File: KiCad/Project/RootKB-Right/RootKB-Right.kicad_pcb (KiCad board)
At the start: 2 copper layers, 137.4 x 107.4 mm, 70 parts, among them J1 OLED-128x32, SW1 Switch, U1 Arduino_Pro_Micro, U2 TRRS

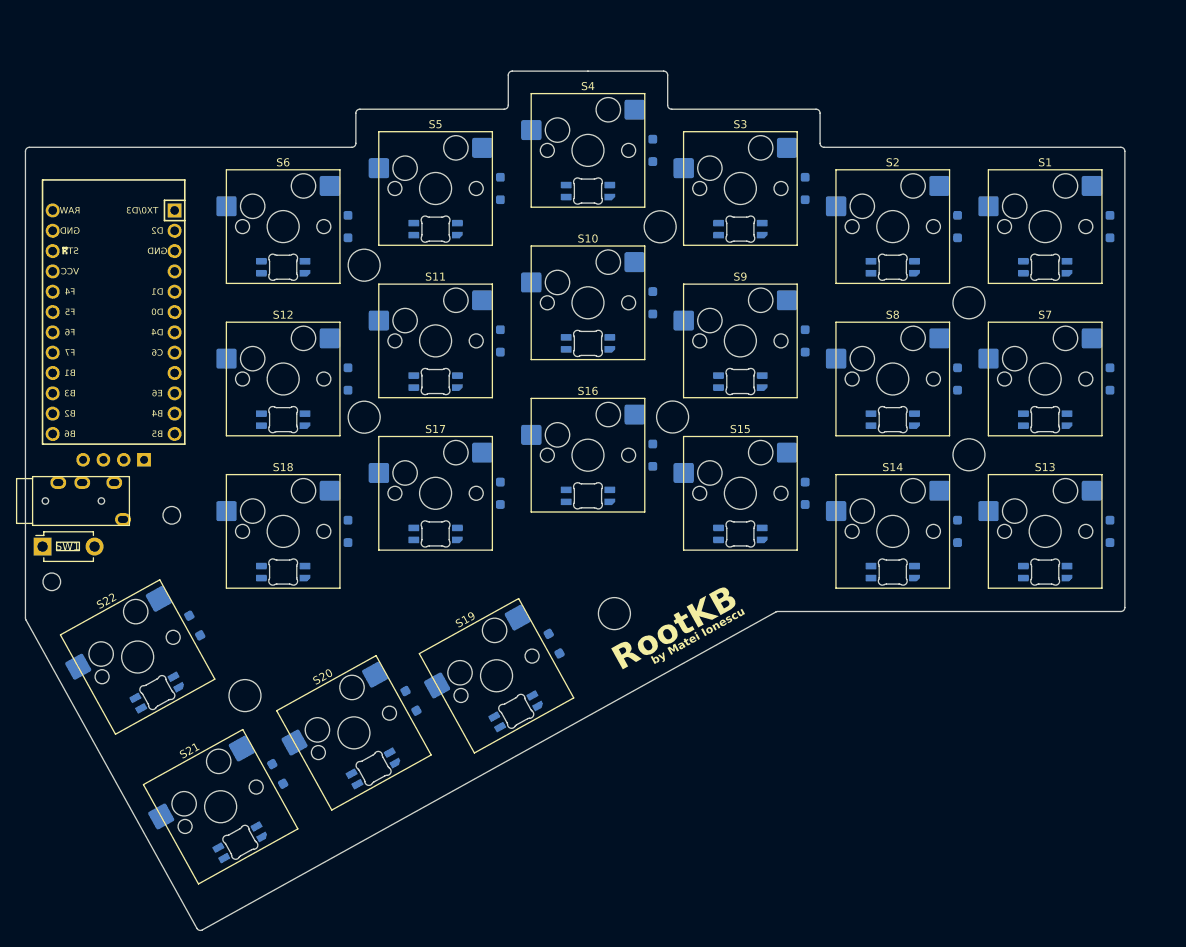
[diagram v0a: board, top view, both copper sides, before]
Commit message: Make symmetrical right PCB
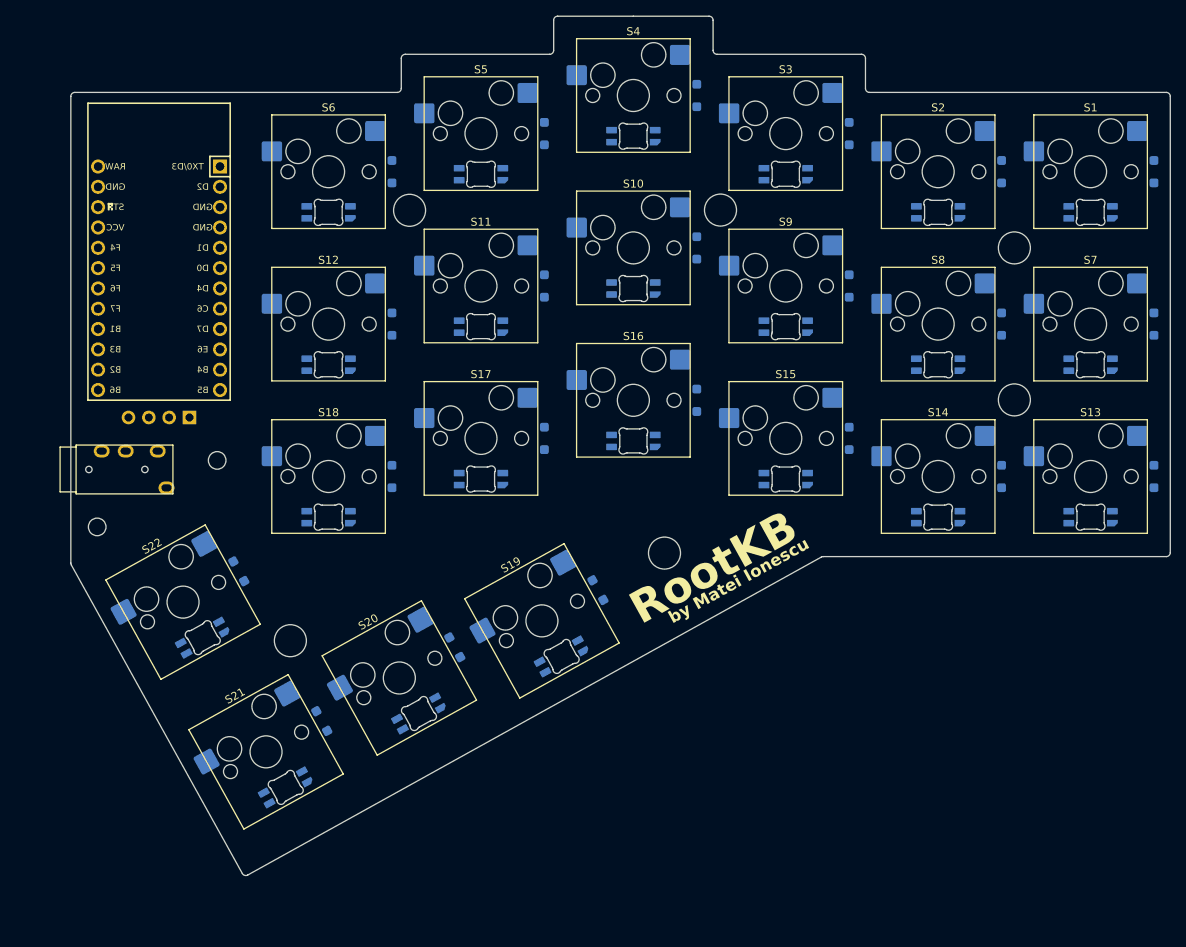
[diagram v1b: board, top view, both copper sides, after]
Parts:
- removed SW1: Switch, ScottoKeebs_Components:Button_MJTP1250
- moved LED21 8.90 mm to (108.8, 136.0)
- moved LED15 8.90 mm to (171.3, 97.4)
- moved LED19 8.90 mm to (143.3, 119.6)
- moved LED3 8.90 mm to (171.3, 59.3)
- moved LED9 8.90 mm to (171.3, 78.4)
- moved S15 8.90 mm to (171.3, 92.3)
- moved S3 8.90 mm to (171.3, 54.2)
- moved S9 8.90 mm to (171.3, 73.3)
- moved S6 8.90 mm to (114.2, 59.0)
- moved LED12 8.90 mm to (114.2, 83.1)
- moved LED18 8.90 mm to (114.2, 102.2)
- moved LED20 8.90 mm to (125.5, 126.7)
- moved LED6 8.90 mm to (114.2, 64.1)
- moved S12 8.90 mm to (114.2, 78.0)
- moved S18 8.90 mm to (114.2, 97.1)
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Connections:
- D10 pad 1: Row 3 -> Row 1
- D11 pad 1: Row 0 -> Row 1
- D14 pad 1: Row 3 -> Row 2
- D15 pad 1: Row 0 -> Row 2
- D16 pad 1: Row 1 -> Row 2
- D18 pad 1: Row 3 -> Row 2
- D19 pad 1: Row 0 -> Row 3
- D2 pad 1: Row 1 -> Row 0
- D20 pad 1: Row 1 -> Row 3
- D21 pad 1: Row 2 -> Row 3
- D3 pad 1: Row 2 -> Row 0
- D5 pad 1: Row 1 -> Row 0
- D6 pad 1: Row 2 -> Row 0
- D7 pad 1: Row 0 -> Row 1
- D9 pad 1: Row 2 -> Row 1
- LED1 pad 3: LED -> Net-(LED1-DIN)
- LED10 pad 2: unconnected-(LED10-DOUT-Pad2) -> Net-(LED10-DOUT)
- LED11 pad 3: Net-(LED11-DIN) -> Net-(LED10-DOUT)
- LED12 pad 3: Net-(LED12-DIN) -> Net-(LED11-DOUT)
- LED14 pad 2: Net-(LED10-DIN) -> Net-(LED13-DIN)
- LED15 pad 2: Net-(LED15-DOUT) -> Net-(LED14-DIN)
- LED15 pad 3: Net-(LED11-DOUT) -> Net-(LED15-DIN)
- LED16 pad 2: Net-(LED12-DIN) -> Net-(LED15-DIN)
- LED17 pad 2: Net-(LED17-DOUT) -> Net-(LED16-DIN)
- LED17 pad 3: Net-(LED13-DOUT) -> Net-(LED17-DIN)
- LED18 pad 2: Net-(LED14-DIN) -> Net-(LED17-DIN)
- LED18 pad 3: Net-(LED18-DIN) -> Net-(LED12-DOUT)
- LED19 pad 3: Net-(LED15-DOUT) -> Net-(LED13-DOUT)
- LED2 pad 2: Net-(LED2-DOUT) -> Net-(LED1-DIN)
- LED20 pad 2: Net-(LED16-DIN) -> Net-(LED20-DOUT)
- LED21 pad 3: Net-(LED17-DOUT) -> Net-(LED20-DOUT)
- LED22 pad 2: Net-(LED18-DIN) -> unconnected-(LED22-DOUT-Pad2)
- LED3 pad 2: Net-(LED3-DOUT) -> Net-(LED2-DIN)
- LED3 pad 3: Net-(LED2-DOUT) -> Net-(LED3-DIN)
- LED3 pad 4: unconnected-(LED3-VSS-Pad4) -> GND
- LED4 pad 2: Net-(LED4-DOUT) -> Net-(LED3-DIN)
- LED4 pad 3: Net-(LED1-DOUT) -> Net-(LED4-DIN)
- LED5 pad 2: Net-(LED2-DIN) -> Net-(LED4-DIN)
- LED6 pad 2: Net-(LED6-DOUT) -> Net-(LED5-DIN)
- LED6 pad 3: Net-(LED3-DOUT) -> LED
- LED6 pad 4: unconnected-(LED6-VSS-Pad4) -> GND
- LED7 pad 2: Net-(LED11-DIN) -> Net-(LED7-DOUT)
- LED7 pad 3: Net-(LED4-DOUT) -> Net-(LED1-DOUT)
- LED8 pad 2: Net-(LED5-DIN) -> Net-(LED8-DOUT)
- LED8 pad 3: Net-(LED12-DOUT) -> Net-(LED7-DOUT)
- LED9 pad 2: Net-(LED13-DIN) -> Net-(LED10-DIN)
- LED9 pad 3: Net-(LED6-DOUT) -> Net-(LED8-DOUT)
- S10 pad 1: Column 2 -> Column 3
- S11 pad 1: Column 3 -> Column 4
- S12 pad 1: Column 3 -> Column 5
- S13 pad 1: Column 3 -> Column 0
- S14 pad 1: Column 3 -> Column 1
- S15 pad 1: Column 4 -> Column 2
- S16 pad 1: Column 4 -> Column 3
- S18 pad 1: Column 4 -> Column 5
- S19 pad 1: Column 5 -> Column 2
- S2 pad 1: Column 0 -> Column 1
- S20 pad 1: Column 5 -> Column 3
- S21 pad 1: Column 5 -> Column 4
- S3 pad 1: Column 0 -> Column 2
- S4 pad 1: Column 1 -> Column 3
- S5 pad 1: Column 1 -> Column 4
- S6 pad 1: Column 1 -> Column 5
- S7 pad 1: Column 2 -> Column 0
- S8 pad 1: Column 2 -> Column 1
- U1 pad 1: unconnected-(U1-TX0/PD3-Pad1) -> TRRS_TX
- U1 pad 13: Column 4 -> Column 1
- U1 pad 14: Column 3 -> Column 2
- U1 pad 15: Column 2 -> Column 3
- U1 pad 16: Column 1 -> Column 4
- U1 pad 2: TRRS_SERIAL -> TRRS_RX
- U1 pad 22: RST -> unconnected-(U1-RST-Pad22)
- U2 pad 1: unconnected-(U2-SLEEVE-Pad1) -> GND
- U2 pad 3: GND -> TRRS_RX
- U2 pad 4: TRRS_SERIAL -> TRRS_TX
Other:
- outline, holes or cut-outs redrawn
- board text added: "JLCJLCJLCJLC"

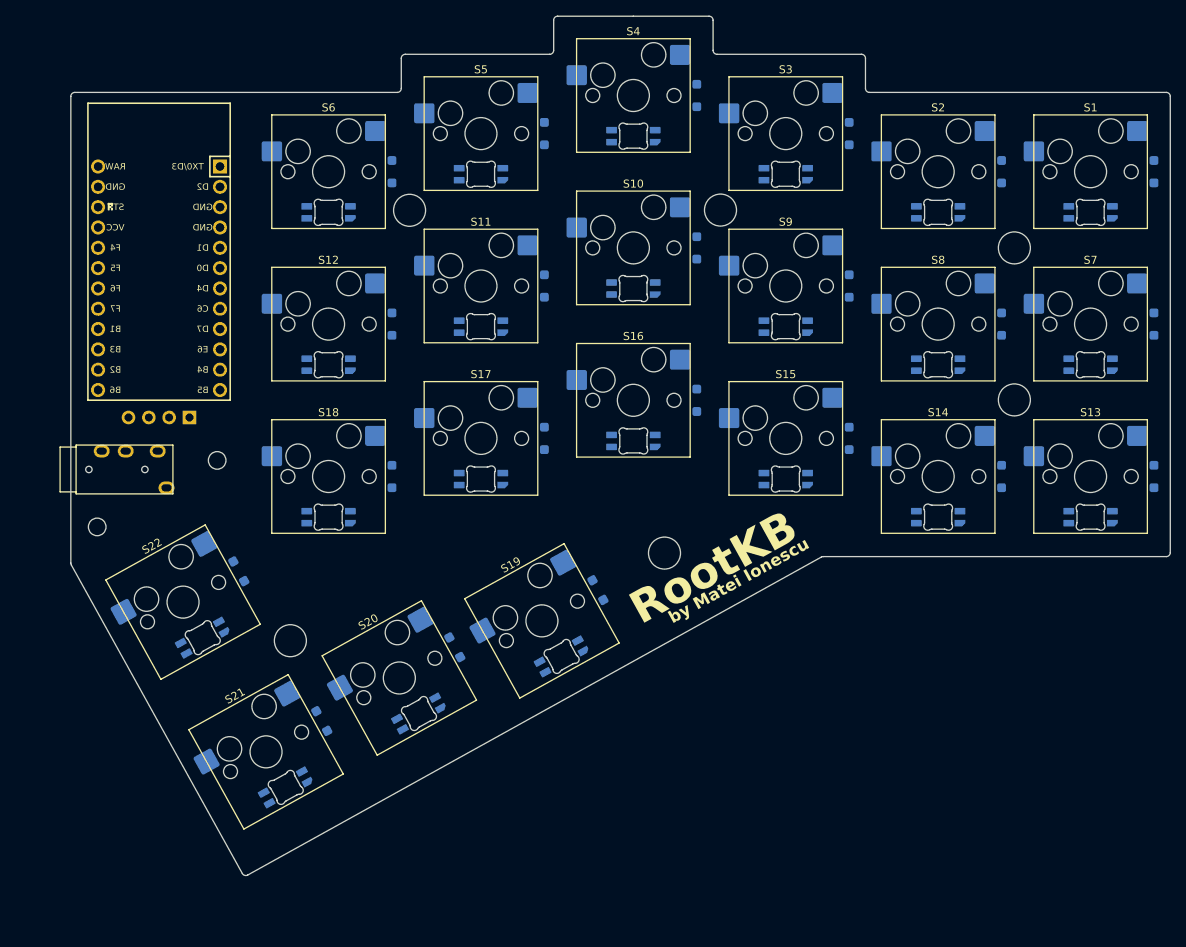
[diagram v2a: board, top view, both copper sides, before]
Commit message: route tracks on right side
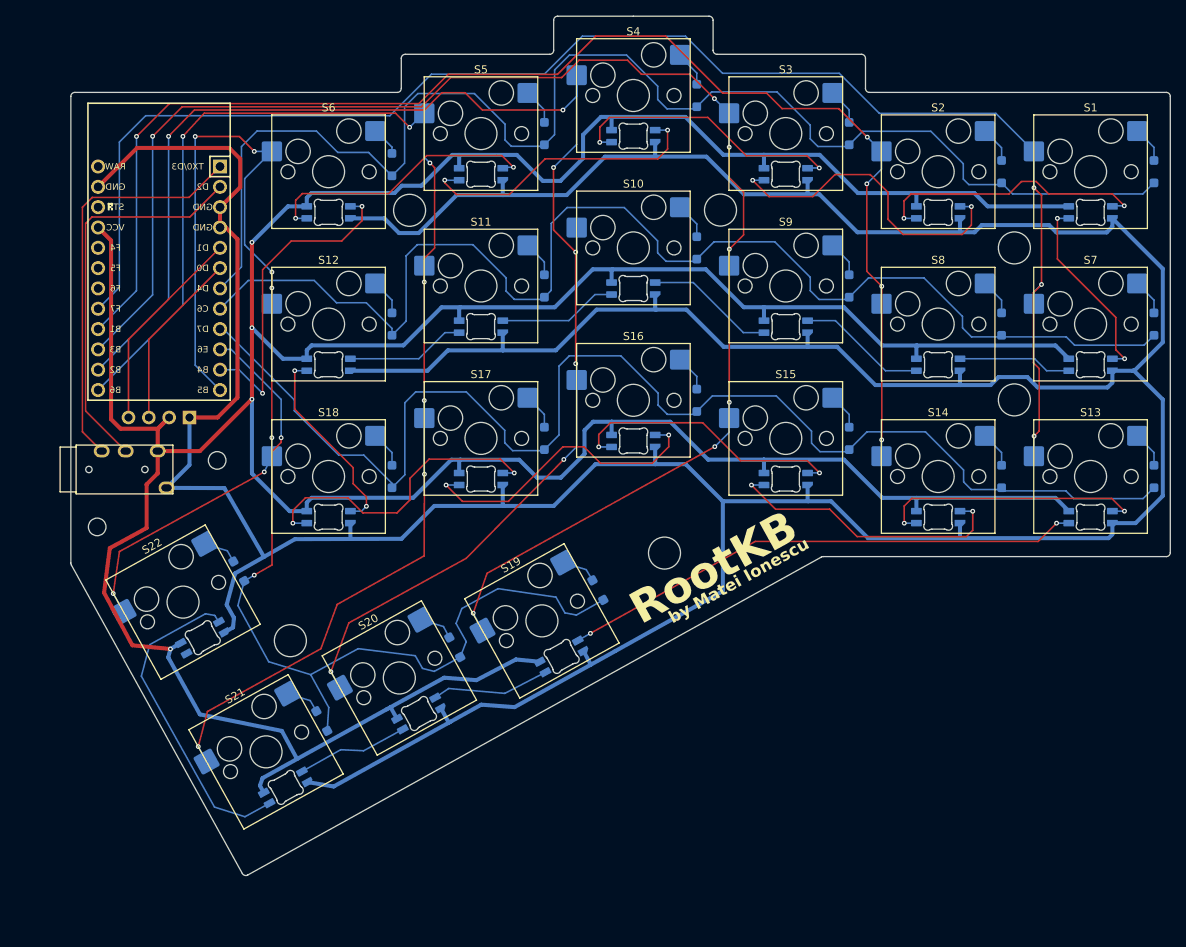
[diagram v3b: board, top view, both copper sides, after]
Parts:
- moved D6 0.89 mm to (122.1, 58.1)
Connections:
- U1 pad 13: Column 1 -> Column 4
- U1 pad 14: Column 2 -> Column 3
- U1 pad 15: Column 3 -> Column 2
- U1 pad 16: Column 4 -> Column 1
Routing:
- net GND: track 0.00 -> 576.3 mm
- net VCC: track 0.00 -> 551.4 mm, vias 0 -> 4
- net Column 2: track 0.00 -> 194.5 mm, vias 0 -> 7
- net Column 0: track 0.00 -> 190.0 mm, vias 0 -> 3
- net Column 3: track 0.00 -> 187.5 mm, vias 0 -> 7
- net Column 1: track 0.00 -> 172.2 mm, vias 0 -> 5
- net Row 0: track 0.00 -> 172.1 mm
- net Column 4: track 0.00 -> 168.7 mm, vias 0 -> 7
- net Row 2: track 0.00 -> 164.9 mm
- net Row 1: track 0.00 -> 159.2 mm
- net Column 5: track 0.00 -> 117.0 mm, vias 0 -> 7
- net Row 3: track 0.00 -> 107.4 mm, vias 0 -> 2
- net Net-(LED13-DOUT): track 0.00 -> 65.6 mm, vias 0 -> 2
- net TRRS_TX: track 0.00 -> 50.8 mm
- net TRRS_RX: track 0.00 -> 49.2 mm
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
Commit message: update routing
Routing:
- net GND: track 576.3 -> 565.2 mm
- net TRRS_RX: track 49.2 -> 58.1 mm
- net TRRS_TX: track 50.8 -> 56.9 mm
- net VCC: track 551.4 -> 551.9 mm
